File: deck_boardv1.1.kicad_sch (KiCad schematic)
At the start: 25 parts, among them J1 D-Sub 15 Pin Female Socket, U1 Raspberry Pi Zero 2 W, U2 LT8610AC, U3 XBP24-Z7SIT-004, U4 ADP7158ARDZ-3.3-R7

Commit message: Updated files and include work done for PCB
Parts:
- C10, C11, C12, C2, C3, C4, C6, C7, C8, C9: footprint (none) -> Capacitor_SMD:C_0603_1608Metric
- C5: value 10nF -> 10pF; footprint (none) -> Capacitor_SMD:C_0603_1608Metric
- D6, D8: footprint (none) -> LED_SMD:LED_0603_1608Metric
- J1: symbol Connector:DA15_Socket -> Connector:DA15_Pins
- L3: footprint (none) -> Inductor_SMD:L_Vishay_IHLP-2525
- R15, R16, R17, R18, R19, R20: footprint (none) -> Resistor_SMD:R_0201_0603Metric
- U3: footprint XBP24-Z7SIT-004:XBP24-Z7SIT-004 -> XBee:XBP24-Z7SIT-004
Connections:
- net TE_3: now reaches J1.11 (P111)
- net TE-RB: now reaches J1.3
- net TE_1: now reaches J1.4
- net GSE 2: now reaches J1.9 (P9)
- new net TE-RA: J1.2
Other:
- moved on the sheet: Reference: J1

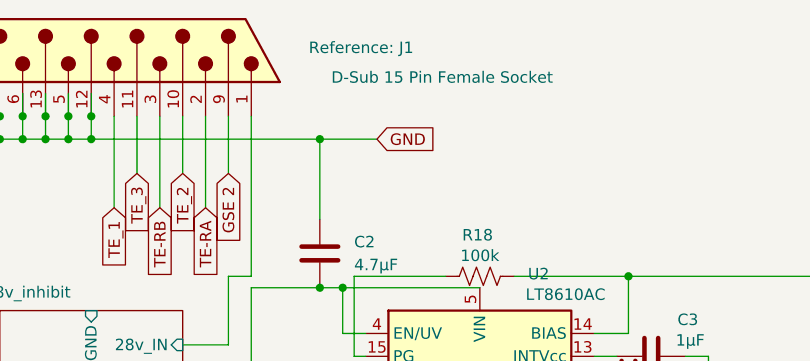
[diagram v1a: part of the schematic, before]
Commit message: Adjusted PCB so that D-sub and burn-element are off the board.
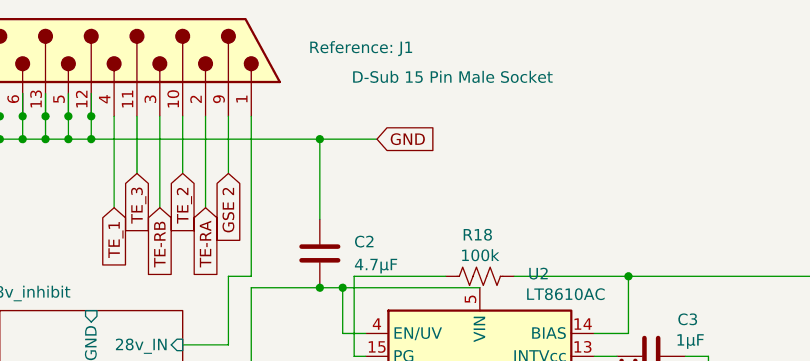
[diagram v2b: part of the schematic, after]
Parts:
- J1: value D-Sub 15 Pin Female Socket -> D-Sub 15 Pin Male Socket
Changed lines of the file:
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@@
 			)
 		)
-		(property "Value" "D-Sub 15 Pin Female Socket"
+		(property "Value" "D-Sub 15 Pin Male Socket"
 			(at 102.108 27.432 90)
 			(effects
